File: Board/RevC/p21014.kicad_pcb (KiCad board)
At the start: 2 copper layers, 59.6 x 25.4 mm, 29 parts, among them J1 Conn_01x06_Male, J3 Conn_02x03_Counter_Clockwise, J4 Conn_01x08_Female, J5 Conn_01x12_Female, J6 Conn_01x06_Female, SW1 SW_Push

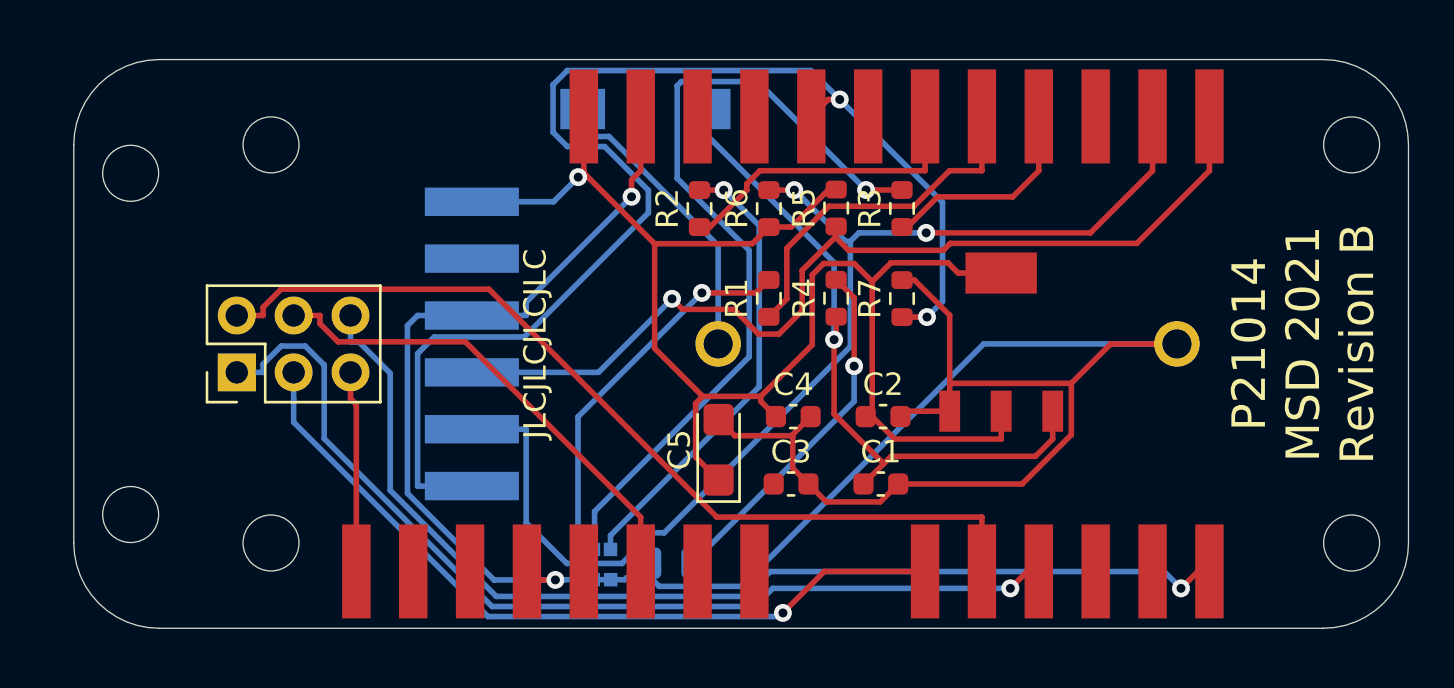
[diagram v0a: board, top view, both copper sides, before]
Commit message: Fixed RevC Layout Alignment
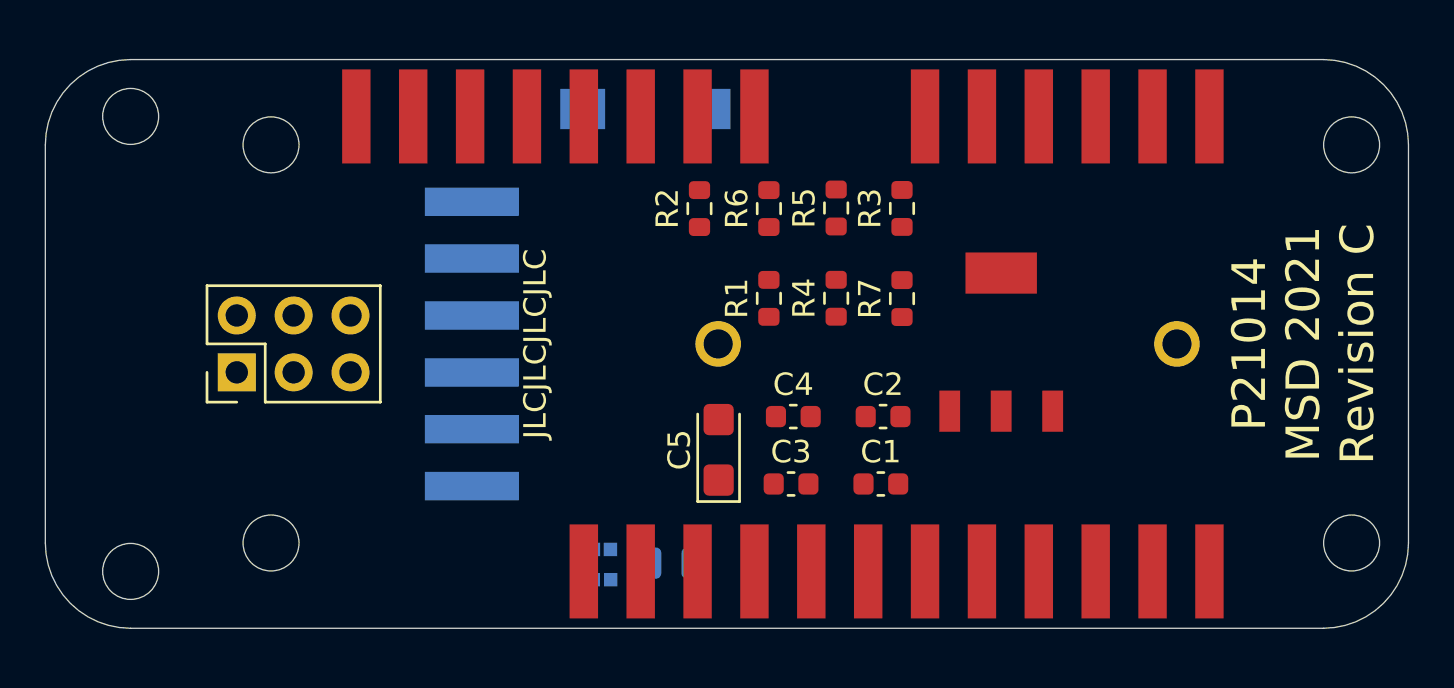
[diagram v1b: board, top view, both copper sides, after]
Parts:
- moved J4 20.3 mm to (179.8, 50.0)
- moved J5 20.3 mm to (190.0, 70.3)
- moved J6 20.3 mm to (205.2, 50.0)
- moved MH6 2.54 mm to (169.8, 50.0)
- moved MH5 2.54 mm to (169.8, 70.3)
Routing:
- net GNDREF: track 109.8 -> 0.00 mm, vias 2 -> 0
- net +5V: track 67.1 -> 0.00 mm, vias 1 -> 0
- net /RST: track 57.9 -> 0.00 mm, vias 2 -> 0
- net /SCL: track 52.5 -> 0.00 mm, vias 2 -> 0
- net Net-(J3-Pad6): track 48.4 -> 0.00 mm, vias 1 -> 0
- net Net-(J3-Pad1): track 43.9 -> 0.00 mm, vias 1 -> 0
- net /SDA: track 42.4 -> 0.00 mm, vias 1 -> 0
- net Net-(J3-Pad2): track 40.6 -> 0.00 mm
- net Net-(D1-Pad2): track 37.0 -> 0.00 mm, vias 1 -> 0
- net Net-(J3-Pad3): track 34.9 -> 0.00 mm, vias 1 -> 0
- net +BATT: track 30.7 -> 0.00 mm, vias 1 -> 0
- net Net-(J3-Pad4): track 21.9 -> 0.00 mm
- net Net-(D1-Pad3): track 20.5 -> 0.00 mm, vias 1 -> 0
- net Net-(D1-Pad1): track 17.0 -> 0.00 mm, vias 1 -> 0
- net Net-(D2-Pad2): track 16.0 -> 0.00 mm, vias 1 -> 0
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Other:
- board size 59.6 x 25.4 mm -> 60.9 x 25.4 mm
- board text added: "P21014 MSD 2021 Revision C"
- board text removed: "P21014 MSD 2021 Revision B"

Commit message: Fixed RevC Outline and STP/DSN
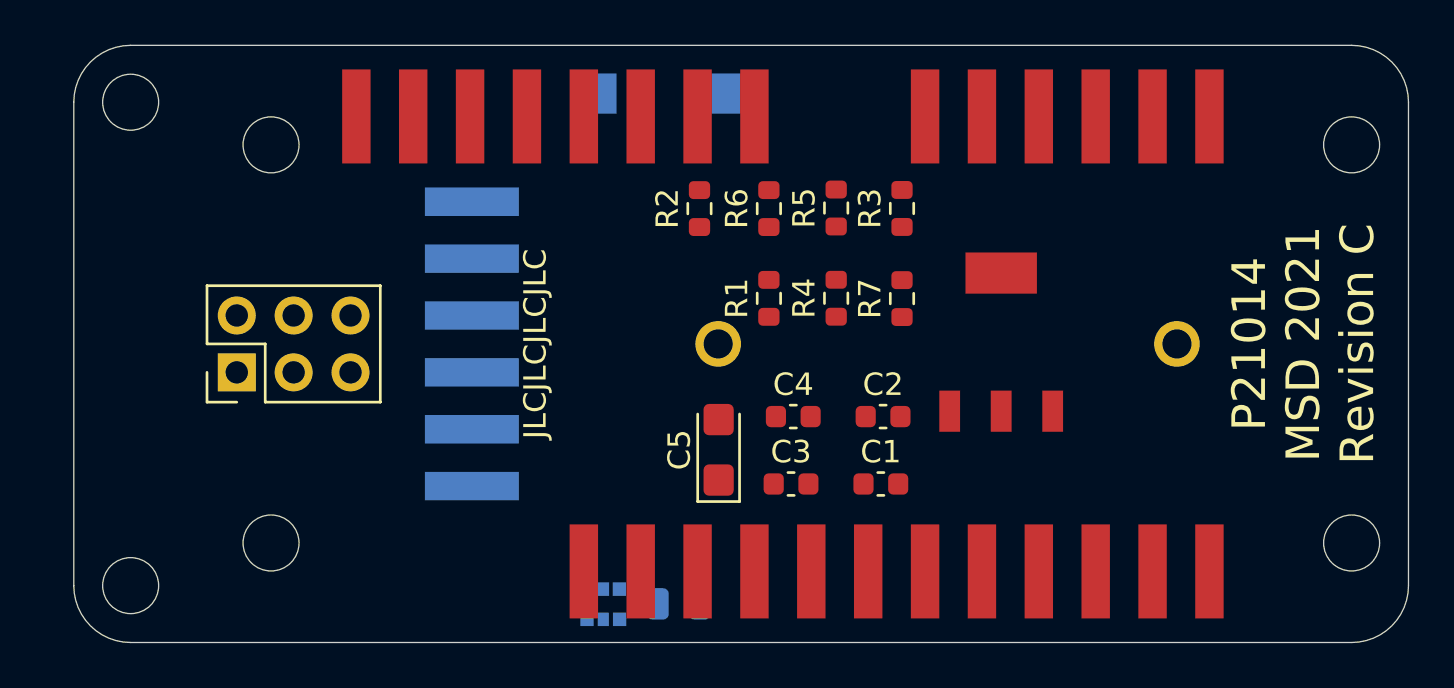
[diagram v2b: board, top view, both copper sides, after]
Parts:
- moved D2 1.85 mm to (194.2, 71.8)
- moved D1 1.81 mm to (190.1, 72.5)
- moved SW1 0.86 mm to (190.5, 49.0)
- moved MH5 0.64 mm to (169.8, 71.0)
- moved MH6 0.63 mm to (169.8, 49.4)
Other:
- board size 60.9 x 25.4 mm -> 59.6 x 26.7 mm
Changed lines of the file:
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@@
   )
   (module 0_MSD_FPs:LED_0805_2012Metric (layer B.Cu)
-    (at 193.91 69.95)
+    (at 194.24 71.77)
     (descr "LED SMD 0805 (2012 Metric), square (rectangular) end terminal, IPC_7351 nominal, (Body size source: https://docs.google.com/spreadsheets/d/1BsfQQcO9C6DZCsRaXUlFlo91Tg2WpOkGARC1WS5S8t0/edit?usp=sharing), generated with kicad-footprint-generator")
     (tags LED)
@@
   )
   (module MountingHole:MountingHole_2.5mm (layer F.Cu)
-    (at 169.76 70.32)
+    (at 169.76 70.955)
     (descr "Mounting Hole 2.5mm, no annular")
     (tags "mounting hole 2.5mm no annular")
@@
   )
   (module MountingHole:MountingHole_2.5mm (layer F.Cu)
-    (at 169.76 50)
+    (at 169.76 49.365)
     (descr "Mounting Hole 2.5mm, no annular")
     (tags "mounting hole 2.5mm no annular")
@@
   )
   (module 0_MSD_FPs:RGB_AJS (layer B.Cu)
-    (at 189.74 70.69)
+    (at 190.14 72.46)
     (fp_text reference D1 (at 0.75 -0.65) (layer Cmts.User)
       (effects (font (size 0.2 0.2) (thickness 0.05)))
@@
   )
   (module 0_MSD_FPs:AJS-Switch_CFS-0102TA (layer B.Cu)
-    (at 189.95 49.67 270)
+    (at 190.46 48.98 270)
     (fp_text reference SW1 (at 0.635 -2.54 270) (layer Cmts.User)
       (effects (font (size 1 1) (thickness 0.15)))
@@
     )
   )
-  (gr_line (start 165.95 69.05) (end 165.95 51.27) (layer Edge.Cuts) (width 0.05))
-  (gr_arc (start 169.76 69.05) (end 165.95 69.05) (angle -90) (layer Edge.Cuts) (width 0.05))
-  (gr_arc (start 169.76 51.27) (end 169.76 47.46) (angle -90) (layer Edge.Cuts) (width 0.05))
+  (gr_line (start 167.22 70.955) (end 167.22 49.365) (layer Edge.Cuts) (width 0.05))
+  (gr_arc (start 169.76 70.955) (end 167.22 70.955) (angle -90) (layer Edge.Cuts) (width 0.05))
+  (gr_arc (start 169.76 49.365) (end 169.76 46.825) (angle -90) (layer Edge.Cuts) (width 0.05))
   (gr_line (start 156.72 60.16) (end 242.06 60.16) (layer Dwgs.User) (width 0.15))
   (gr_line (start 169.76 72.86) (end 169.76 47.46) (layer Dwgs.User) (width 0.05))
@@
     (effects (font (size 1 1) (thickness 0.15)))
   )
-  (gr_arc (start 223.02 69.05) (end 223.02 72.86) (angle -90) (layer Edge.Cuts) (width 0.05))
-  (gr_arc (start 223.02 51.27) (end 226.83 51.27) (angle -90) (layer Edge.Cuts) (width 0.05))
+  (gr_arc (start 224.29 70.955) (end 224.29 73.495) (angle -90) (layer Edge.Cuts) (width 0.05))
+  (gr_arc (start 224.29 49.365) (end 226.83 49.365) (angle -90) (layer Edge.Cuts) (width 0.05))
   (gr_arc (start 177.3 51.27) (end 177.3 47.46) (angle -90) (layer Dwgs.User) (width 0.05))
   (gr_arc (start 177.3 69.05) (end 173.49 69.05) (angle -90) (layer Dwgs.User) (width 0.05))
-  (gr_line (start 226.83 69.05) (end 226.83 51.27) (layer Edge.Cuts) (width 0.05))
+  (gr_line (start 226.83 70.955) (end 226.83 49.365) (layer Edge.Cuts) (width 0.05))
   (gr_line (start 173.49 69.05) (end 173.49 51.27) (layer Dwgs.User) (width 0.05))
-  (gr_line (start 169.76 72.86) (end 223.02 72.86) (layer Edge.Cuts) (width 0.05))
-  (gr_line (start 169.76 47.46) (end 223.02 47.46) (layer Edge.Cuts) (width 0.05))
+  (gr_line (start 169.76 73.495) (end 224.29 73.495) (layer Edge.Cuts) (width 0.05))
+  (gr_line (start 169.76 46.825) (end 224.29 46.825) (layer Edge.Cuts) (width 0.05))
 )

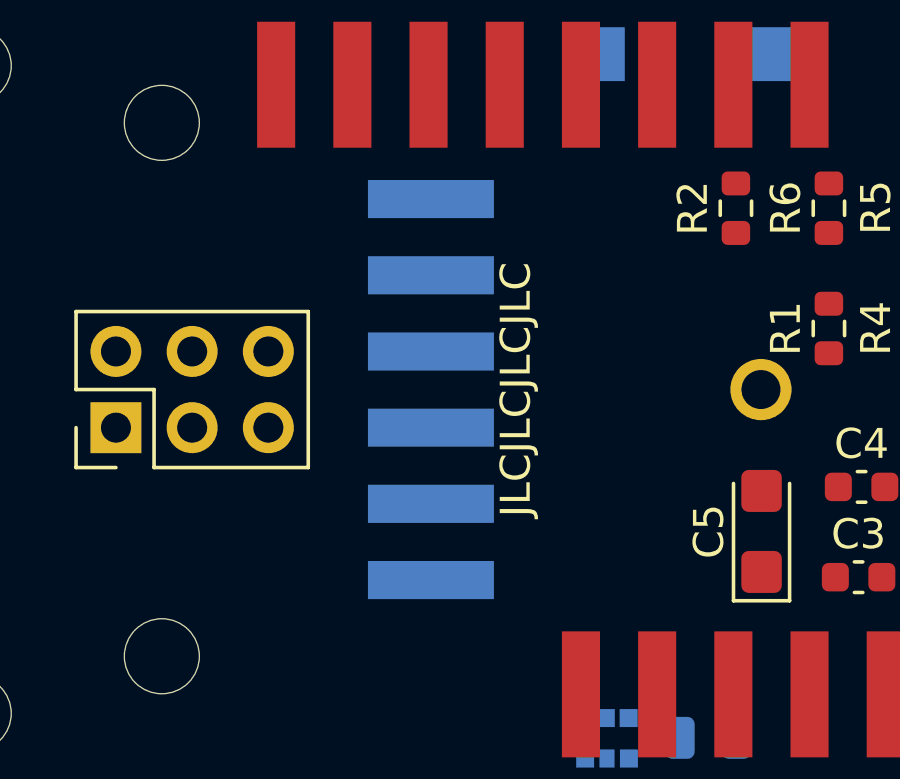
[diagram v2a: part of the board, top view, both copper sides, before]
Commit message: Updated IMU Mounting Location for RevC
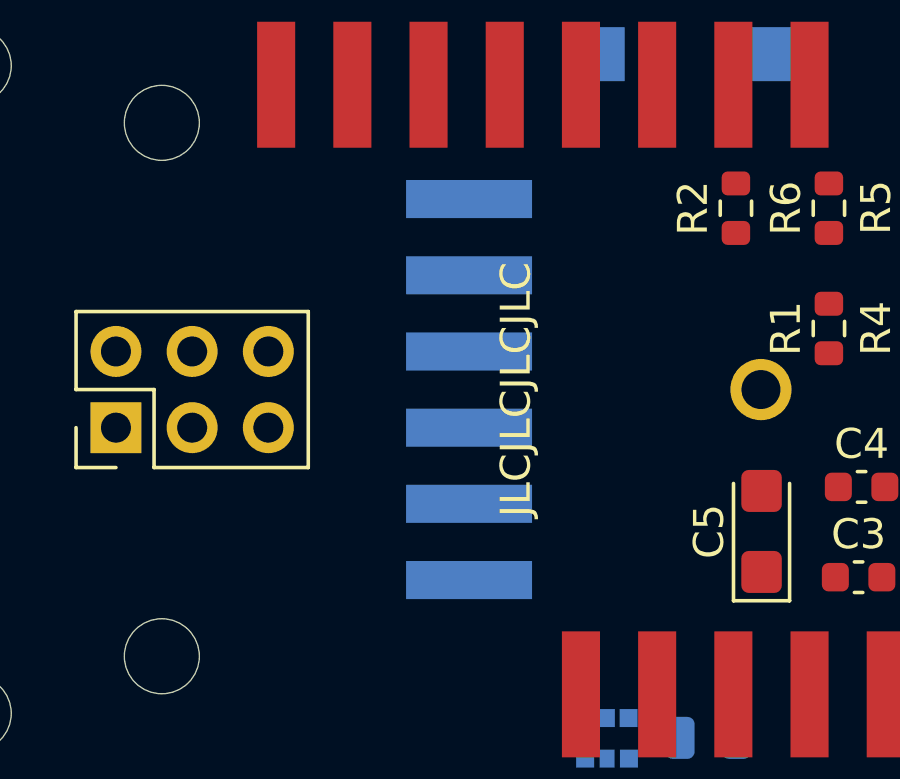
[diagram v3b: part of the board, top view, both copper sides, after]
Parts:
- moved J1 1.27 mm to (186.3, 53.8)
- moved G55 0.22 mm to (191.1, 60.2)
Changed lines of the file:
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@@
   )
   (module 0_MSD_FPs:RIT_Logo (layer B.Cu)
-    (at 190.9 60.16 270)
+    (at 191.12 60.16 270)
     (fp_text reference G55 (at 0 0 270) (layer B.SilkS) hide
       (effects (font (size 1.524 1.524) (thickness 0.3)) (justify mirror))
@@
   )
   (module 0_MSD_FPs:MSD_6_Pin (layer B.Cu)
-    (at 185 53.81 270)
+    (at 186.27 53.81 270)
     (fp_text reference J1 (at 1.27 -3.81 270) (layer Cmts.User)
       (effects (font (size 1 1) (thickness 0.15)))

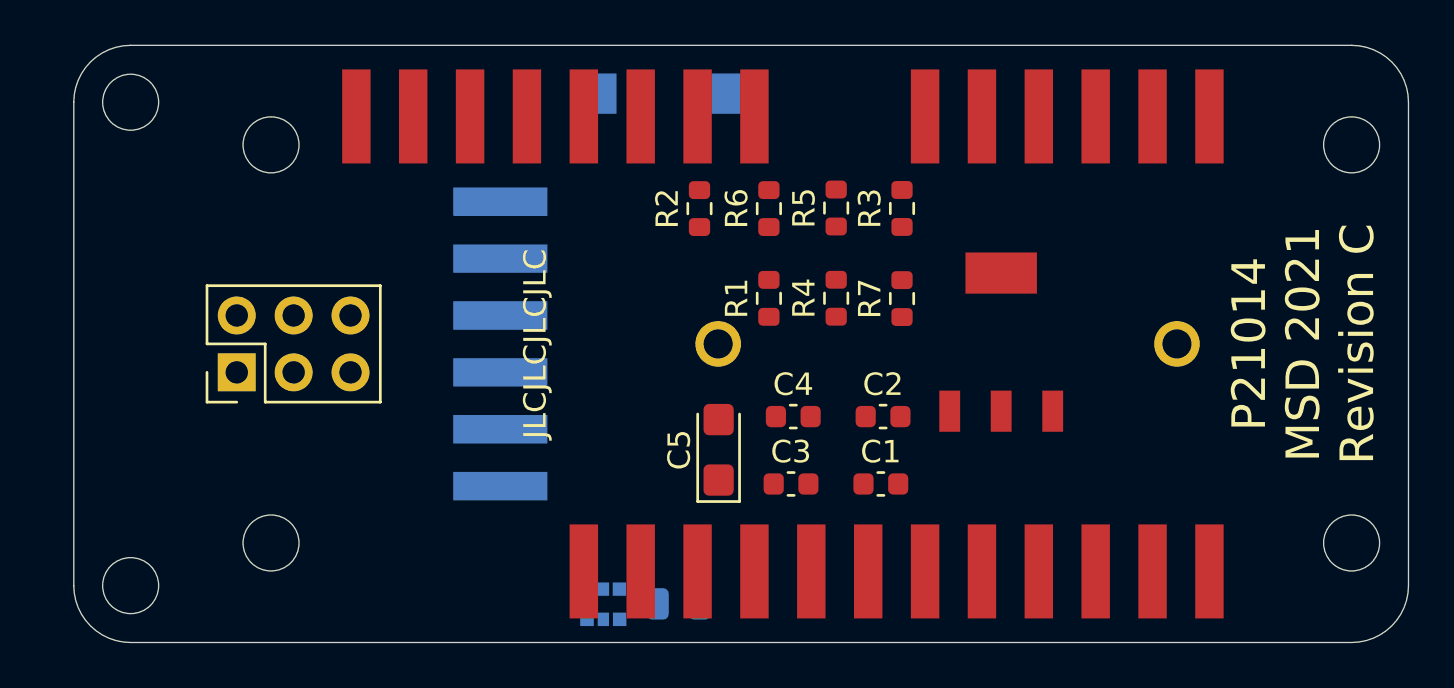
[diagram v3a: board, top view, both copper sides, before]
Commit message: Completed RevC Routing
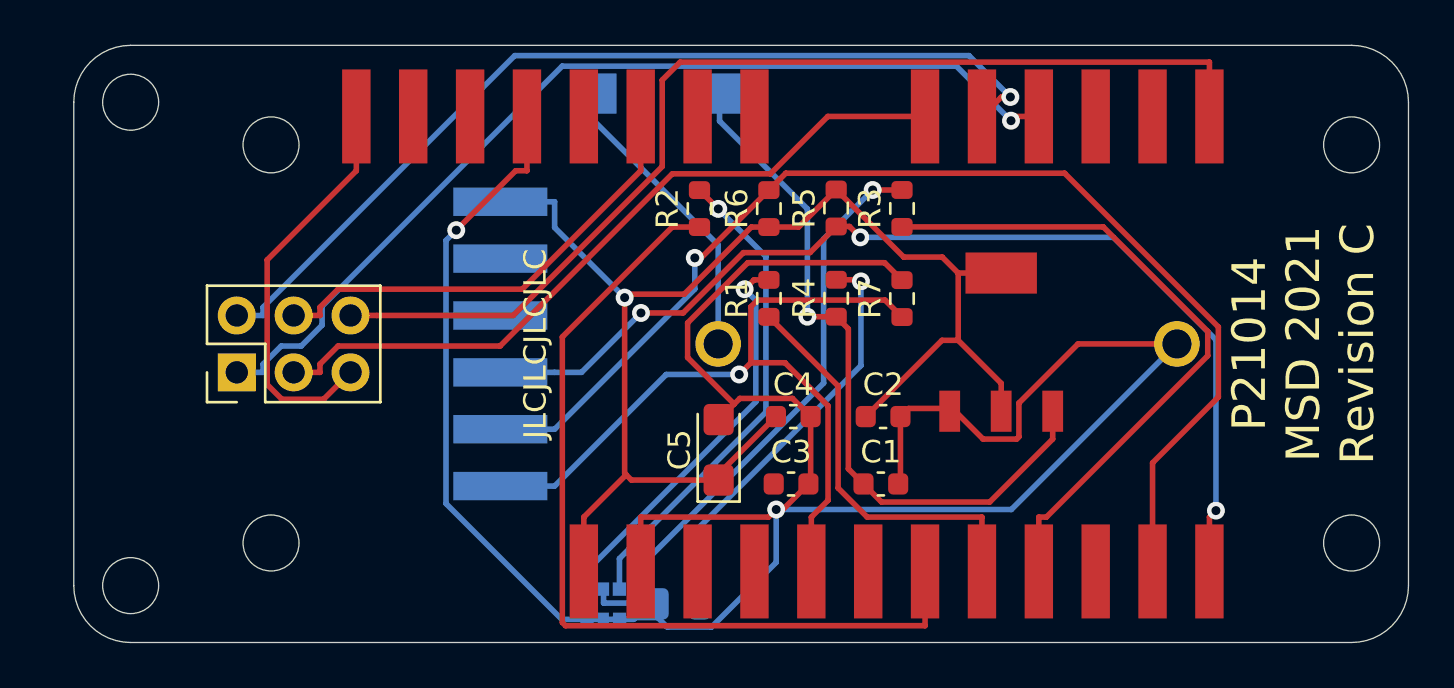
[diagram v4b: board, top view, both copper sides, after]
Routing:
- net GNDREF: track 0.00 -> 116.7 mm, vias 0 -> 2
- net +5V: track 0.00 -> 62.0 mm, vias 0 -> 1
- net /SCL: track 0.00 -> 52.6 mm, vias 0 -> 1
- net Net-(J3-Pad6): track 0.00 -> 47.7 mm
- net /SDA: track 0.00 -> 47.2 mm, vias 0 -> 3
- net Net-(J3-Pad1): track 0.00 -> 43.3 mm, vias 0 -> 1
- net Net-(J3-Pad2): track 0.00 -> 42.0 mm, vias 0 -> 1
- net /Feather_Board/RED: track 0.00 -> 39.6 mm
- net /RST: track 0.00 -> 35.1 mm, vias 0 -> 1
- net Net-(J3-Pad3): track 0.00 -> 33.1 mm
- net +BATT: track 0.00 -> 32.0 mm, vias 0 -> 1
- net /Feather_Board/BLUE: track 0.00 -> 29.6 mm
- net Net-(D1-Pad2): track 0.00 -> 26.0 mm, vias 0 -> 1
- net Net-(D1-Pad3): track 0.00 -> 21.8 mm, vias 0 -> 1
- net Net-(J3-Pad4): track 0.00 -> 20.8 mm
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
